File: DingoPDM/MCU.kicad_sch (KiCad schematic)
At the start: 39 parts, among them J5 TC, SW1 SW_SPDT, U10 PCA82C250, U11 TLP172AM, U12 W25Q32JVSSIQ_TR, U9 STM32F303CCTx, Y1 8mHz, Y2 32.768kHz

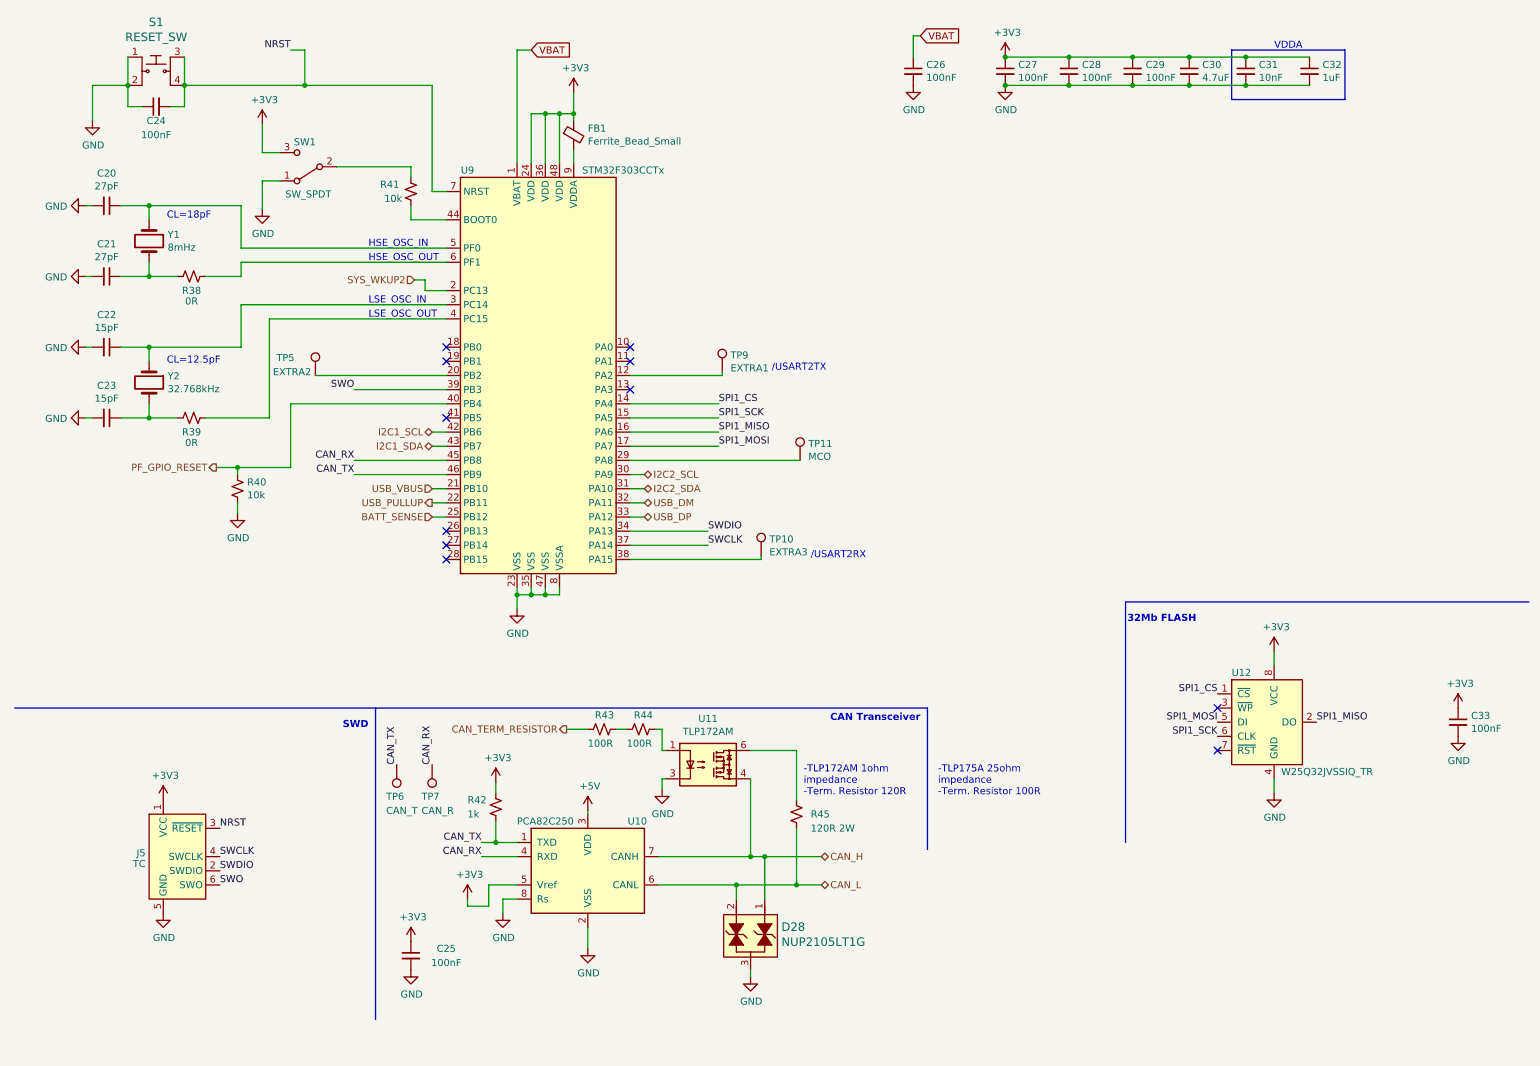
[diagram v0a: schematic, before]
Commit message: Changed schematic sheet size to letter
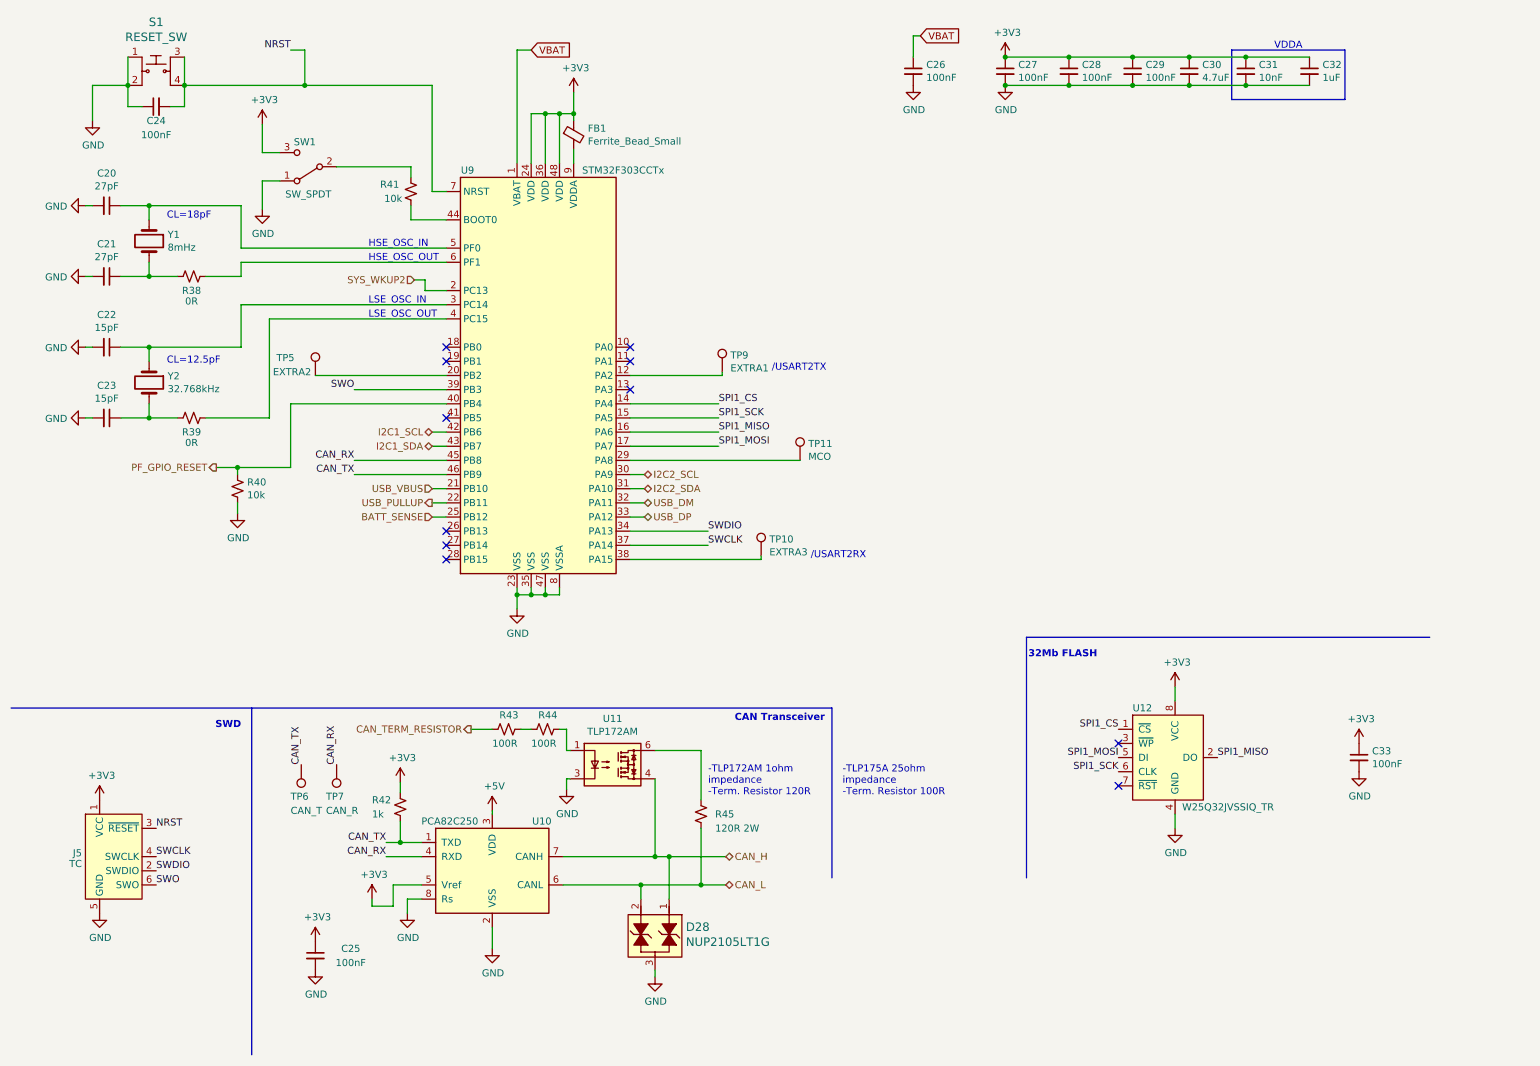
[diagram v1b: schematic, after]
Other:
- moved on the sheet: C25, C33, D28, J5, R42, R43, R44, R45, TP6, TP7, U10, U11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

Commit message: Redesigned to a smaller unit
4x high current, 2x med current, 4x low current, 2x digital inputs
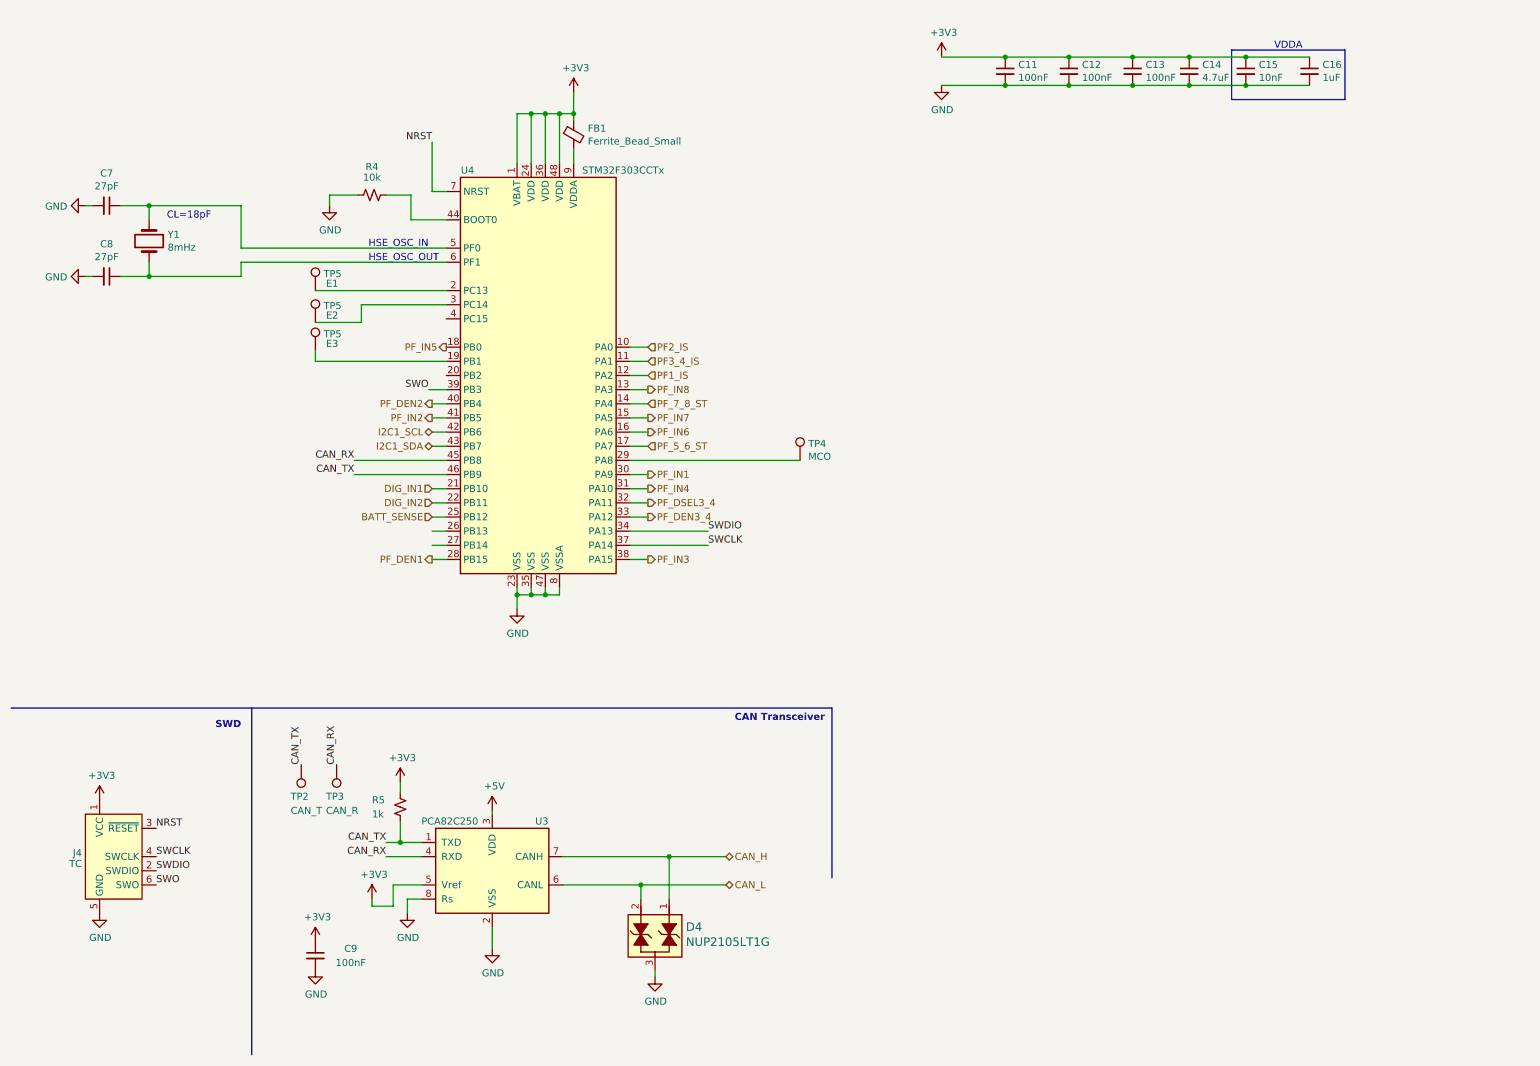
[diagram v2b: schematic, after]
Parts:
- removed C22, C23: 15pF, Capacitor_SMD:C_0805_2012Metric, symbol Device:C_Small
- removed C24, C26, C33: 100nF, Capacitor_SMD:C_0805_2012Metric, symbol Device:C_Small
- removed R38, R39: 0R, Resistor_SMD:R_0805_2012Metric, symbol Device:R_Small_US
- removed R40: 10k, Resistor_SMD:R_0805_2012Metric, symbol Device:R_Small_US
- removed R43, R44: 100R, Resistor_SMD:R_0805_2012Metric, symbol Device:R_Small_US
- removed R45: 120R 2W, Resistor_SMD:R_2512_6332Metric, symbol Device:R_Small_US
- removed S1: RESET_SW, digikey-footprints:Switch_Tactile_SMD_6x6mm, symbol dk_Tactile-Switches:FSM4JSMATR
- removed SW1: SW_SPDT, SlideSwitch:CJS-1200TB, symbol Switch:SW_SPDT
- removed TP10: EXTRA3, TestPoint:TestPoint_Keystone_5000-5004_Miniature, symbol Connector:TestPoint
- removed TP5: EXTRA2, TestPoint:TestPoint_Keystone_5000-5004_Miniature, symbol Connector:TestPoint
- removed TP9: EXTRA1, TestPoint:TestPoint_Keystone_5000-5004_Miniature, symbol Connector:TestPoint
- removed U11: TLP172AM, Package_SO:MFSOP6-4_4.4x3.6mm_P1.27mm, symbol Relay_SolidState:TLP175A
- removed U12: W25Q32JVSSIQ_TR, digikey-footprints:SOIC-8_W5.6mm, symbol dk_Memory:W25Q32JVSSIQ_TR
- removed Y2: 32.768kHz, Crystals_Modify:Crystal_SMD_3215-2Pin_3.2x1.5mm_HandSoldering, symbol Device:Crystal
- added TP5: E1, TestPoint:TestPoint_Keystone_5000-5004_Miniature, symbol Connector:TestPoint
- added TP5: E2, TestPoint:TestPoint_Keystone_5000-5004_Miniature, symbol Connector:TestPoint
- added TP5: E3, TestPoint:TestPoint_Keystone_5000-5004_Miniature, symbol Connector:TestPoint
- C11: renamed from C27; LCSC (none) -> C49678
- C12: renamed from C28; LCSC (none) -> C49678
- C13: renamed from C29; LCSC (none) -> C49678
- C14: renamed from C30; LCSC (none) -> C1779
- C15: renamed from C31; LCSC (none) -> C1710
- C16: renamed from C32; LCSC (none) -> C28323
- C7: renamed from C20; LCSC (none) -> C1808
- C8: renamed from C21; LCSC (none) -> C1808
- C9: renamed from C25; LCSC (none) -> C49678
- D4: renamed from D28; LCSC (none) -> C2976509
- FB1: LCSC (none) -> C85840
- R4: renamed from R41; LCSC (none) -> C17414
- R5: renamed from R42; LCSC (none) -> C17513
- U3: renamed from U10; LCSC (none) -> C7439
- U4: renamed from U9; LCSC (none) -> C81523
- Y1: LCSC (none) -> C144380
- renumbered J5 to J4, TP6 to TP2, TP7 to TP3, TP11 to TP4
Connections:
- net VBAT is gone; now on net +3V3: U4.1 (VBAT)
- net GND: now also R4.2
- net PF2_IS: now reaches U4.10 (PA0)
- net PF3_4_IS: now reaches U4.11 (PA1)
- net PF1_IS: now reaches U4.12 (PA2)
- net PF_IN8: now reaches U4.13 (PA3)
- net PF_IN5: now reaches U4.18 (PB0)
- net at U4.19 (PB1): now also TP5.1
- net PF_DEN1: now reaches U4.28 (PB15)
- net at U4.3 (PC14): now also TP5.1
- net PF_IN3: now reaches U4.38 (PA15)
- net PF_IN2: now reaches U4.41 (PB5)
- net at U4.44 (BOOT0): now also R4.1; no longer R4.2
- net at U4.6 (PF1): now also C8.1, Y1.2
- net I2C2_SCL renamed PF_IN1
- net I2C2_SDA renamed PF_IN4
- net PF_GPIO_RESET renamed PF_DEN2
- net SPI1_CS renamed PF_7_8_ST
- net SPI1_MISO renamed PF_IN6
- net SPI1_MOSI renamed PF_5_6_ST
- net SPI1_SCK renamed PF_IN7
- net SYS_WKUP2: no longer names the net of U4.2 (PC13)
- net SYS_WKUP2: now also TP5.1
- net USB_DM renamed PF_DSEL3_4
- net USB_DP renamed PF_DEN3_4
- net USB_PULLUP renamed DIG_IN2
- net USB_VBUS renamed DIG_IN1
- no-connect marks 11 -> 0
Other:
- note removed: "-TLP172AM 1ohm impedance -Term. Resistor 120R"
- note removed: "-TLP175A 25ohm impedance -Term. Resistor 100R"
- note removed: "/USART2RX"
- note removed: "/USART2TX"
- note removed: "32Mb FLASH"
- note removed: "CL=12.5pF"
- note removed: "LSE_OSC_IN"
- note removed: "LSE_OSC_OUT"
- moved on the sheet: R4
